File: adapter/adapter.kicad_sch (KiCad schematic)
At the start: 16 parts, among them J1 DF3A-2P-2DSA, J10 Ribbon, J11 Ribbon, J12 Ribbon, J2 DF3A-2P-2DSA, J9 Ribbon, SW1 CAS-120TA, SW2 CAS-120TA, U1 nice_nano, U2 nice_nano

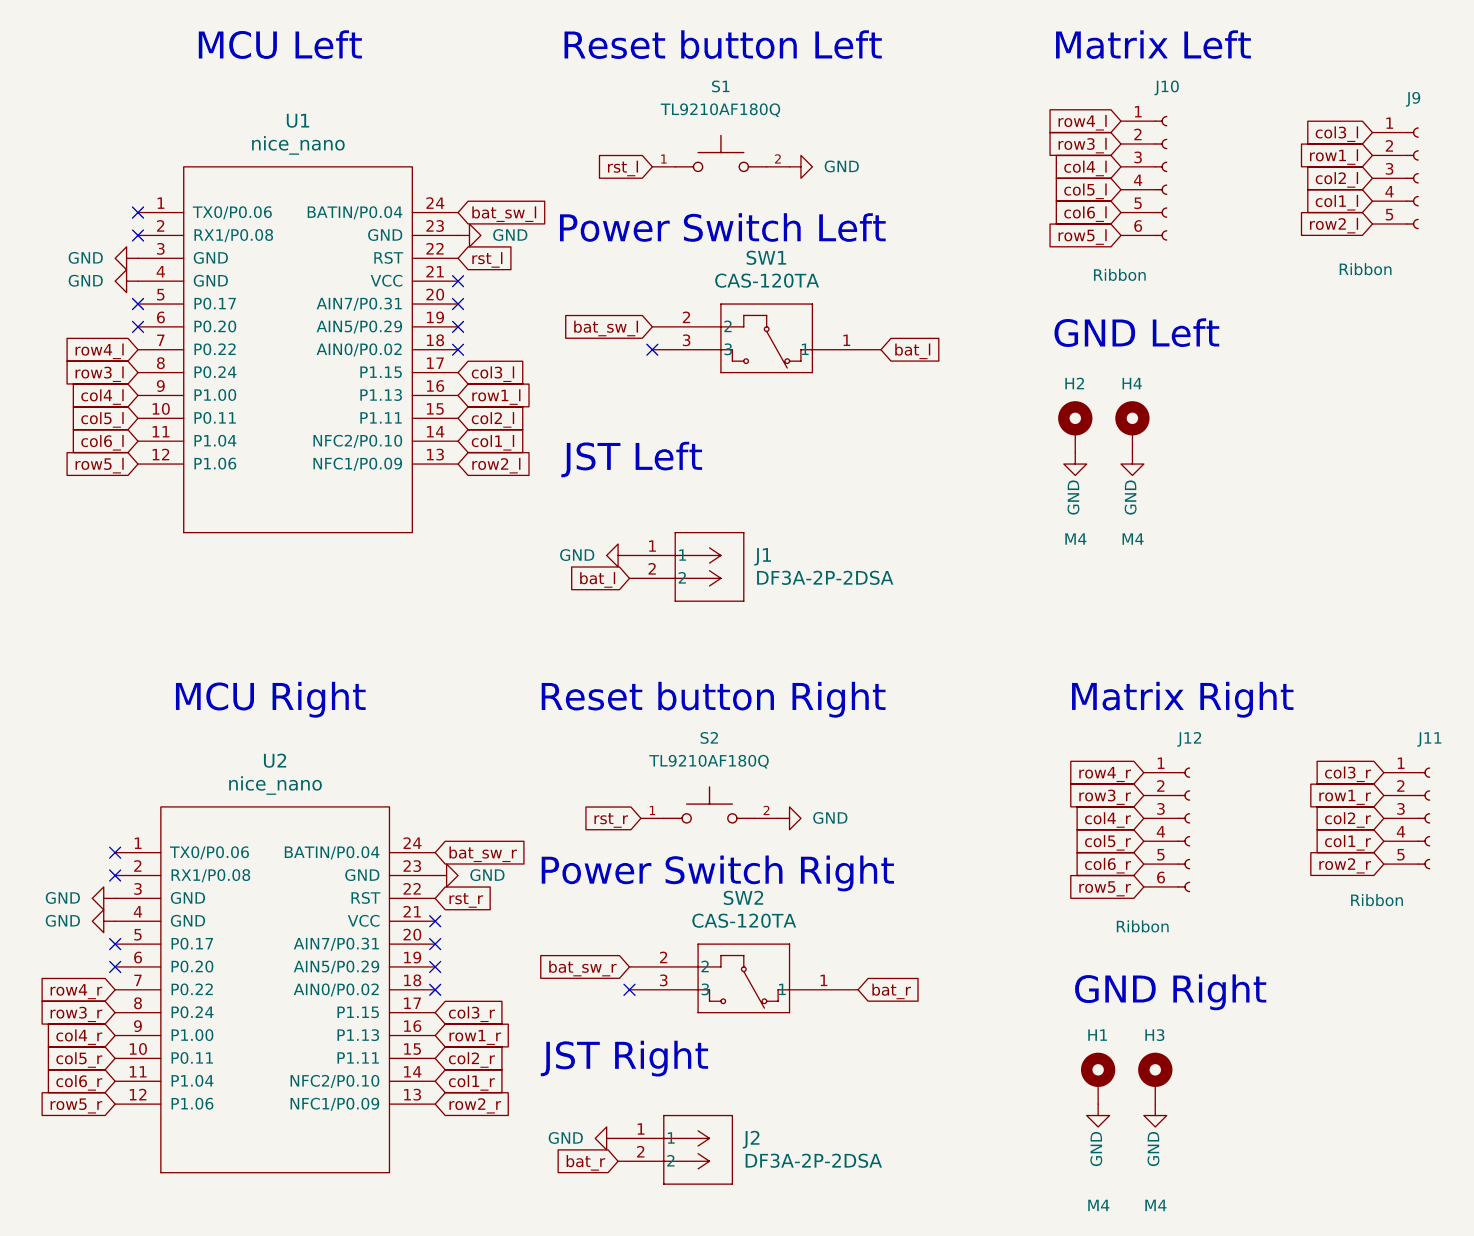
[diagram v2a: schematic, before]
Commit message: Solve all ERC errors
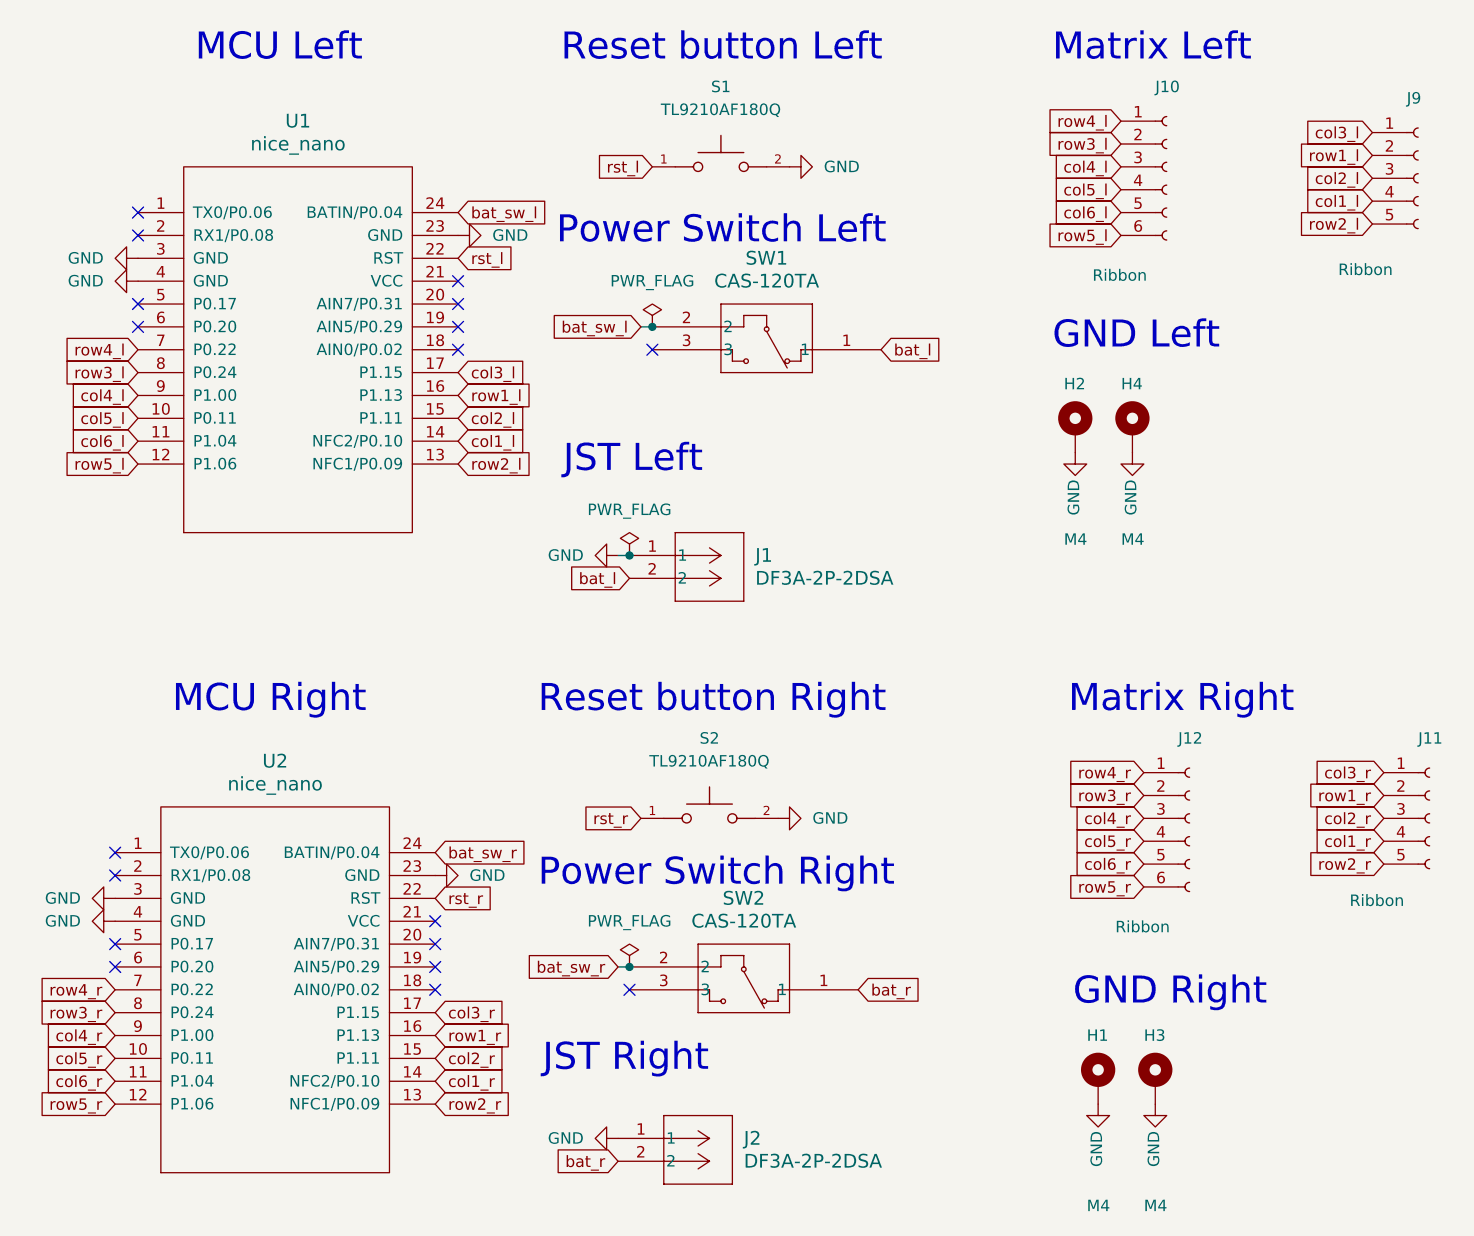
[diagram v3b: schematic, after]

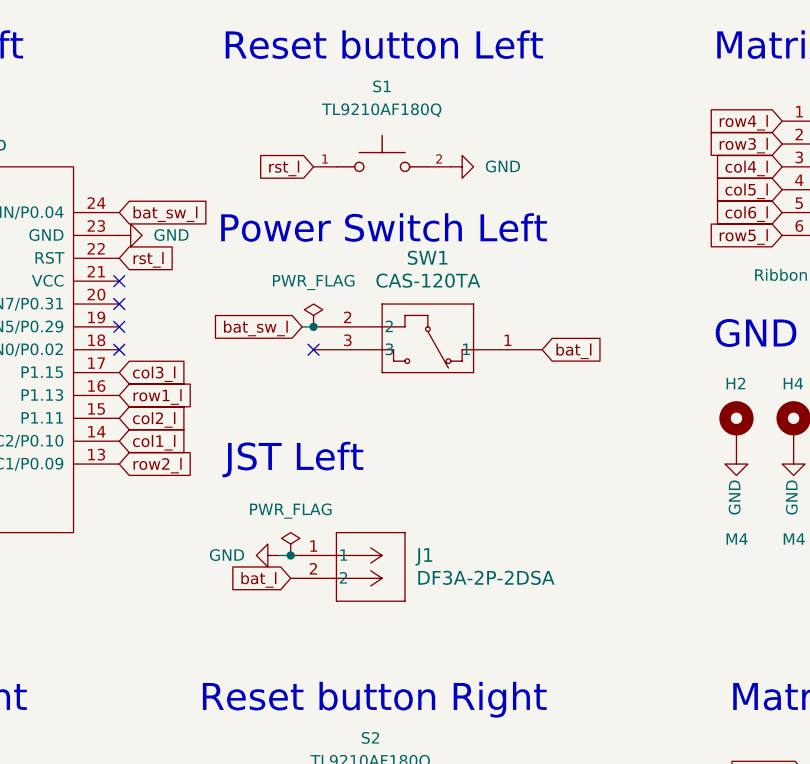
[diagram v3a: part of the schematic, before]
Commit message: Removed the powerswitch, reset button and jst connector + fixed the corner extention
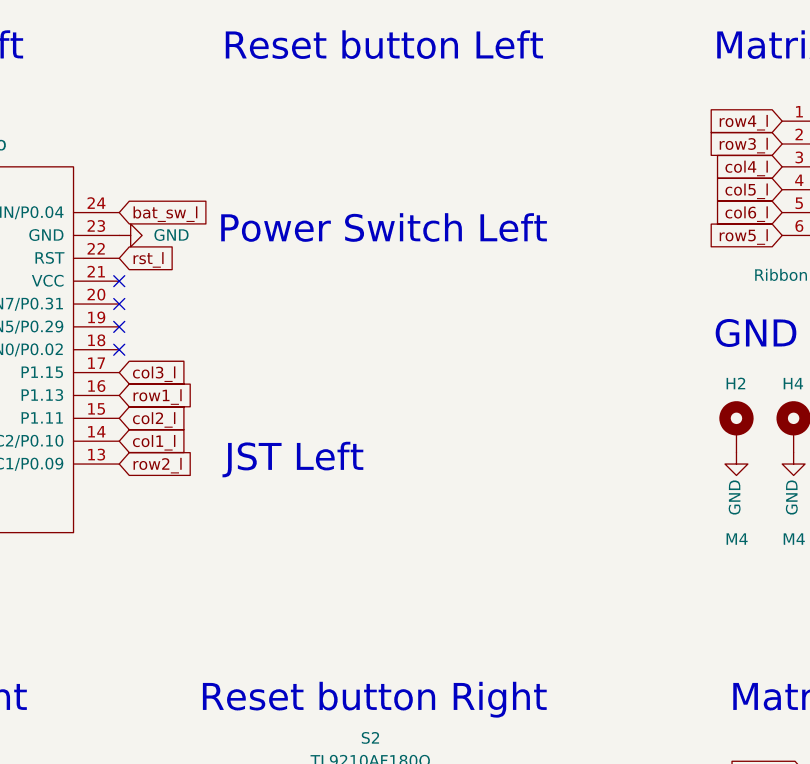
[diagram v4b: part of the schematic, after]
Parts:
- removed J1: DF3A-2P-2DSA, Library:DF3A_2P_2DSA, symbol DF3A_2P_2DSA:DF3A-2P-2DSA
- removed S1: TL9210AF180Q, Library:SW_TL9210AF180Q, symbol TL9210AF180Q:TL9210AF180Q
- removed SW1: CAS-120TA, Library:CAS-120A_NDC, symbol CAS-120TA:CAS-120TA
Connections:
- no-connect marks 18 -> 17

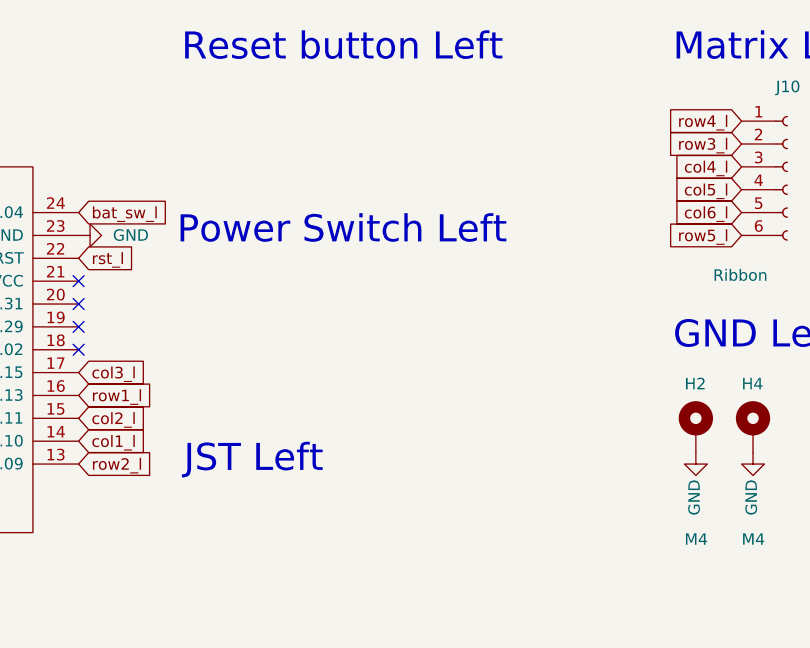
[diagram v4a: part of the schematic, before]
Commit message: Add custom reset switch
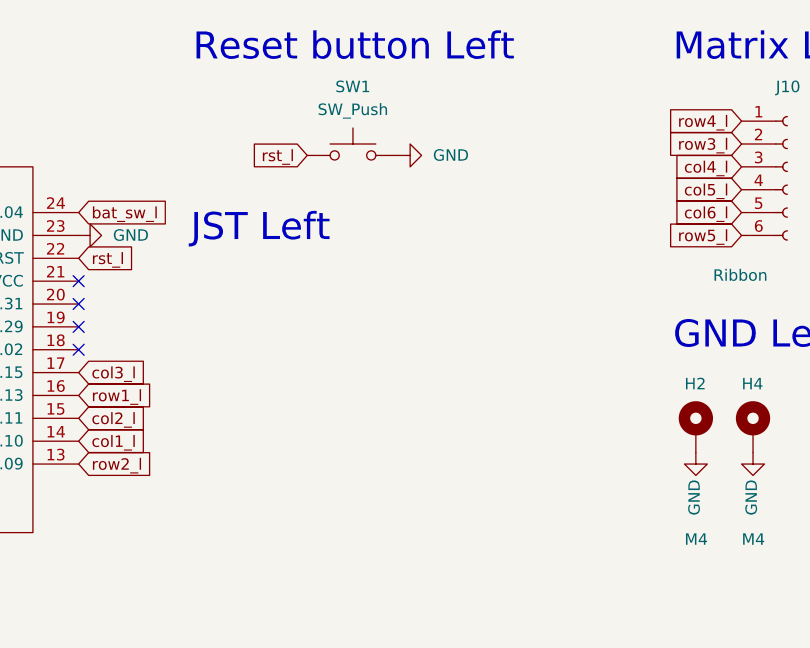
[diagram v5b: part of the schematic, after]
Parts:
- added SW1: SW_Push, Library:SW_Tactile_3x3_SMD_H1p5, symbol Switch:SW_Push
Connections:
- net GND: now also SW1.2
- net rst_l: now also SW1.1
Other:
- note removed: "Power Switch Left"
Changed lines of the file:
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@@
 	(text "Reset button Left"
 		(exclude_from_sim no)
-		(at 77.47 27.94 0)
+		(at 78.74 27.94 0)
 		(effects
 			(font
@@
 	(text "JST Left"
 		(exclude_from_sim no)
-		(at 77.724 73.66 0)
-		(effects
-			(font
-				(size 3 3)
-			)
-			(justify left bottom)
-		)
-	)
-	(text "Power Switch Left"
-		(exclude_from_sim no)
-		(at 76.962 48.26 0)
+		(at 78.486 48.006 0)
 		(effects
 			(font
@@
 		(property "Intersheetrefs" "${INTERSHEET_REFS}"
 			(at -1.27 76.2 0)
+			(effects
+				(font
+					(size 1.27 1.27)
+				)
+				(hide yes)
+			)
+		)
+	)
+	(global_label "rst_l"
+		(shape input)
+		(at 91.44 38.1 180)
+		(effects
+			(font
+				(size 1.27 1.27)
+			)
+			(justify right)
+		)
+		(property "Intersheetrefs" "${INTERSHEET_REFS}"
+			(at 62.23 -29.21 0)
 			(effects
 				(font
@@
 	)
 	(symbol
+		(lib_id "Switch:SW_Push")
+		(at 96.52 38.1 0)
+		(unit 1)
+		(exclude_from_sim no)
+		(in_bom yes)
+		(on_board yes)
+		(dnp no)
+		(fields_autoplaced yes)
+		(property "Reference" "SW1"
+			(at 96.52 30.48 0)
+			(effects
+				(font
+					(size 1.27 1.27)
+				)
+			)
+		)
+		(property "Value" "SW_Push"
+			(at 96.52 33.02 0)
+			(effects
+				(font
+					(size 1.27 1.27)
+				)
+			)
+		)
+		(property "Footprint" "Library:SW_Tactile_3x3_SMD_H1p5"
+			(at 96.52 33.02 0)
+			(effects
+				(font
+					(size 1.27 1.27)
+				)
+				(hide yes)
+			)
+		)
+		(property "Datasheet" "~"
+			(at 96.52 33.02 0)
+			(effects
+				(font
+					(size 1.27 1.27)
+				)
+				(hide yes)
+			)
+		)
+		(property "Description" "Push button switch, generic, two pins"
+			(at 96.52 38.1 0)
+			(effects
+				(font
+					(size 1.27 1.27)
+				)
+				(hide yes)
+			)
+		)
+		(pin "2"
+		)
+		(pin "1"
+		)
+		(instances
+			(project ""
+				(path "/e63e39d7-6ac0-4ffd-8aa3-1841a4541b55"
+					(reference "SW1")
+					(unit 1)
+				)
+			)
+		)
+	)
+	(symbol
 		(lib_id "CAS-120TA:CAS-120TA")
 		(at 110.49 130.81 180)
@@
 					(unit 1)
 				)
+			)
+		)
+	)
+	(symbol
+		(lib_name "GND_2")
+		(lib_id "power:GND")
+		(at 101.6 38.1 90)
+		(unit 1)
+		(exclude_from_sim no)
+		(in_bom yes)
+		(on_board yes)
+		(dnp no)
+		(fields_autoplaced yes)
+		(property "Reference" "#PWR01"
+			(at 107.95 38.1 0)
+			(effects
+				(font
+					(size 1.27 1.27)
+				)
+				(hide yes)
+			)
+		)
+		(property "Value" "GND"
+			(at 105.41 38.0999 90)
+			(effects
+				(font
+					(size 1.27 1.27)
+				)
+				(justify right)
+			)
+		)
+		(property "Footprint" ""
+			(at 101.6 38.1 0)
+			(effects
+				(font
+					(size 1.27 1.27)
+				)
+				(hide yes)
+			)
+		)
+		(property "Datasheet" ""
+			(at 101.6 38.1 0)
+			(effects
+				(font
+					(size 1.27 1.27)
+				)
+				(hide yes)
+			)
+		)
+		(property "Description" "Power symbol creates a global label with name \"GND\" , ground"
+			(at 101.6 38.1 0)
+			(effects
+				(font
+					(size 1.27 1.27)
+				)
+				(hide yes)
+			)
+		)
+		(pin "1"
+		)
+		(instances
+			(project "adapter"
+				(path "/e63e39d7-6ac0-4ffd-8aa3-1841a4541b55"
+					(reference "#PWR01")
+					(unit 1)
+				)
